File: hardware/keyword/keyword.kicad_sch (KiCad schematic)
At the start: 73 parts, among them U1 SZYY0402Y_C434450, U10 STM32WBA54KGUx, U11 STM32WB55RGVx, U12 MLPF-WB-04D3, U13 YZ13515055F-02025-02, U14 CH9329, U15 YZ13515055F-02025-02, U16 XRTC252012S2R2MBCA, U17 SZYY0402Y_C434450, U18 TPS631000DRLR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

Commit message: add in stuff
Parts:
- removed C10: 470nF, Capacitor_SMD:C_0402_1005Metric, symbol Device:C
- removed C11: 10nF, Capacitor_SMD:C_0402_1005Metric, symbol Device:C
- removed C12: 1uF, Capacitor_SMD:C_0402_1005Metric, symbol Device:C
- removed C13, C15, C3, C4, C5, C8: 100nF, Capacitor_SMD:C_0402_1005Metric, symbol Device:C
- removed C14: 4.7uF, Capacitor_SMD:C_0603_1608Metric, symbol Device:C
- removed C7: 10uF, Capacitor_SMD:C_0603_1608Metric, symbol Device:C
- removed U10: STM32WBA54KGUx, Package_DFN_QFN:QFN-32-1EP_5x5mm_P0.5mm_EP3.45x3.45mm, symbol MCU_ST_STM32WB:STM32WBA54KGUx
- removed U14: CH9329, lcsc:SOP-16_L9.9-W3.9-P1.27-LS6.0-BL, symbol lcsc:CH9329
- added CN1, CN5, CN6: YZ00615050R-08, TestPoint:TestPoint_Pad_D2.0mm, symbol lcsc:YZ00615050R-08
- added CN2, CN3, CN4: YZ00615050R-08, lcsc:TESTPOINT-SMD_BD2.0-H5.0, symbol lcsc:YZ00615050R-08
- added R11, R8: 2.2K, Resistor_SMD:R_0402_1005Metric, symbol Device:R
- added TP6, TP7, TP8, TP9: TestPoint, TestPoint:TestPoint_Pad_D1.5mm, symbol Connector:TestPoint
- added U19, U20: YZ37215050R-02025-05, lcsc:SMD_2P_YZ37215050R-02025-05, symbol lcsc:YZ37215050R-02025-05
- TP1, TP2, TP3: footprint TestPoint:TestPoint_Pad_D2.0mm -> TestPoint:TestPoint_Pad_D1.5mm
- TP4, TP5: footprint TestPoint:TestPoint_Pad_3.0x3.0mm -> TestPoint:TestPoint_Pad_2.0x2.0mm
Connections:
- net SCL1 is gone; now on net SCL: U11.7 (PB9), U5.1
- net SDA1 is gone; now on net SDA: U11.6 (PB8), U4.2
- net +3.3V: now also CN1.1, CN2.1, R11.2, R8.2
- net DN: now also U2.1 (D+), TP6.1, U19.2; no longer U2.2 (D-)
- net DP: now also U2.2 (D-), TP7.1, U19.1; no longer U2.1 (D+)
- net GND: now also TP8.1, TP9.1, U20.1, U20.2
- net SCL: now also U15.1, U7.1, CN4.1, CN6.1, R11.1
- net SDA: now also U13.2, U6.2, CN3.1, CN5.1, R8.1
- net SCL2: no longer names the net of U11.12 (PC3)
- net SCL2: no longer U7.1
- net SCL3: no longer names the net of U11.10 (PC1)
- net SCL3: no longer U15.1
- net SDA2: no longer names the net of U11.11 (PC2)
- net SDA2: no longer U6.2
- net SDA3: no longer names the net of U11.9 (PC0)
- net SDA3: no longer U13.2
- no-connect marks 65 -> 47
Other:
- note added: "Buck Converter"
- note added: "Charger"
- note added: "Connectors"
- moved on the sheet: AE1, C1, C16, C17, C18, C19, C2, C20, C21, C22, C23, C24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

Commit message: finished
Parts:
- removed R3: 150, Resistor_SMD:R_0402_1005Metric, symbol Device:R
- removed U1: SZYY0402Y_C434450, lcsc:LED0402-FD_YELLOW, symbol lcsc:SZYY0402Y_C434450
- added C3: 100nF, Capacitor_SMD:C_0402_1005Metric, symbol Device:C
- added CN7, CN8, CN9: YZ00615050R-08, lcsc:TESTPOINT-SMD_BD2.0-H5.0, symbol lcsc:YZ00615050R-08
- added R12, R13, R14: 100R, Resistor_SMD:R_0402_1005Metric, symbol Device:R
- added U10: W25Q16JVUXIQ, lcsc:USON-8_L3.0-W2.0-P0.50-BL-EP, symbol lcsc:W25Q16JVUXIQ
- added U14: XL-1608RGBC, lcsc:LED-SMD_4P-L1.6-W0.8-BL, symbol lcsc:XL-1608RGBC
- R11, R8: value 2.2K -> 4.7K
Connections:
- net +3.3V: now also C3.1, CN7.1, U10.8 (VCC), U14.3 (com)
- net GND: now also U8.8 (OTG), U8.9 (~{CE}), C3.2, CN9.1, U10.4 (GND), U10.9 (EP)
- net SCL: now also R8.1, U11.47 (PB13), U8.6 (SDA); no longer R11.1, U11.7 (PB9)
- net SDA: now also R11.1, U11.48 (PB14), U8.5 (SCL); no longer R8.1, U11.6 (PB8)
- net FLASH_NCS: now reaches U11.17 (PA2)
- net FLASH_NCS: now also U10.1 (~{CS})
- net FLASH_CLK: now reaches U11.18 (PA3)
- net FLASH_CLK: now also U10.6 (CLK)
- net FLASH_IO3: now reaches U11.21 (PA6)
- net FLASH_IO3: now also U10.7 (HOLD#orRESET#(IO3))
- net FLASH_IO2: now reaches U11.22 (PA7)
- net FLASH_IO2: now also U10.3 (WP#(IO2))
- net STATUS_B: now reaches U11.60 (PC12)
- net STATUS_B: now also R14.2
- net STATUS_G: now reaches U11.61 (PD0)
- net STATUS_G: now also R12.2
- net STATUS_R: now reaches U11.62 (PD1)
- net STATUS_R: now also R13.1
- net BB_SWIO: now reaches U11.65 (PB5)
- net BB_SWIO: now also CN8.1
- net LED: no longer names the net of U11.2 (PC13)
- new net: R12.1, U14.2
- new net: R13.2, U14.1
- new net: R14.1, U14.4
- new net FLASH_IO0: U10.5 (DI(IO0)), U11.7 (PB9)
- new net FLASH_IO1: U10.2 (DO(IO1)), U11.6 (PB8)
- no-connect marks 47 -> 39
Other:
- note added: "A modular keyboard controller"
- note added: "Flash"
- note added: "Keyword"
- note added: "Made by @notaroomba"
- note added: "STM32"
- moved on the sheet: C16, C24, L1, L2, R11, R8, TP1, TP2, TP3, TP8, TP9, U11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

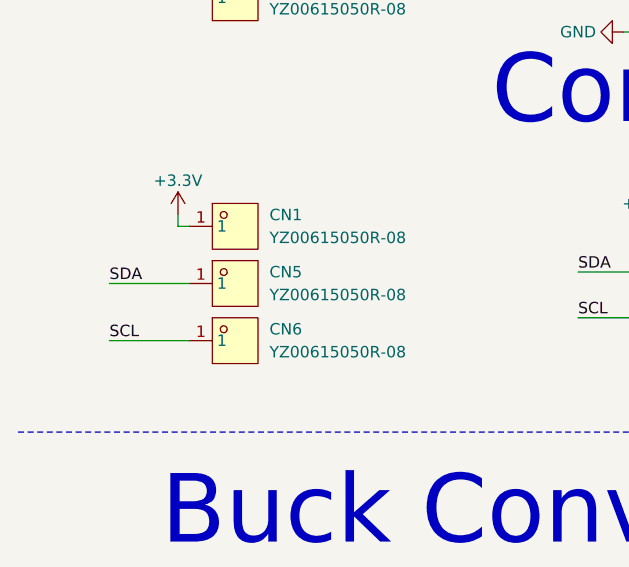
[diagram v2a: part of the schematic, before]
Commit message: add in mousebites
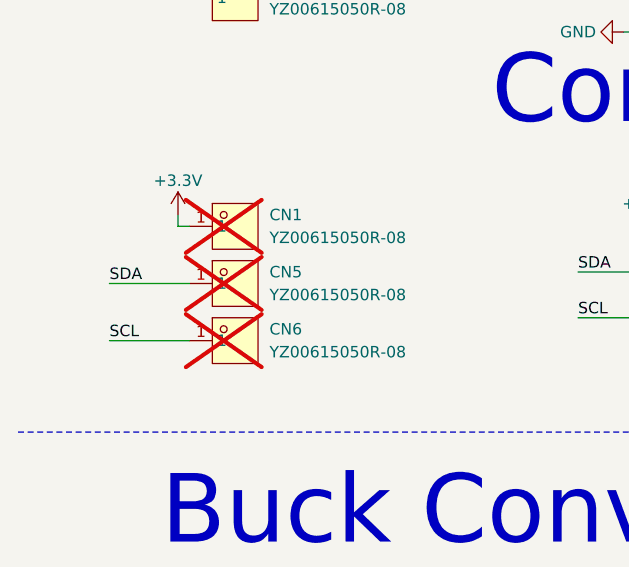
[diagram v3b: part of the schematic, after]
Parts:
- CN1, CN5, CN6: now not fitted
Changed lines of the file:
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@@
 		(in_bom yes)
 		(on_board yes)
-		(dnp no)
+		(dnp yes)
 		(fields_autoplaced yes)
 		(property "Reference" "CN1"
@@
 		(in_bom yes)
 		(on_board yes)
-		(dnp no)
+		(dnp yes)
 		(fields_autoplaced yes)
 		(property "Reference" "CN5"
@@
 		(in_bom yes)
 		(on_board yes)
-		(dnp no)
+		(dnp yes)
 		(fields_autoplaced yes)
 		(property "Reference" "CN6"
